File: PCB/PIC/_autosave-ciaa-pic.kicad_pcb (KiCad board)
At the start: 4 copper layers, 138.8 x 86.3 mm, 442 parts, among them IC1 PS2805-4, IC2 PS2805-4, J1 TB_1X3, J10 TB_1X3, J11 TB_1X2, J12 TB_1X3, J13 TB_1X3, J14 TB_1X2, J15 TB_1X3, J16 TB_1X3, J17 TB_1X2, J18 TB_1X2, J19 TB_1X2, J2 TB_1X3, J3 DB9, J4 TB_1X3, J5 RJ45-TRANSFO, J6 ZX62-AB-5PA, J7 ZX62-AB-5PA, J8 TB_1X3, J9 TB_1X3, K1 RELAY_G5V-2, K2 RELAY_G5V-2, K3 RELAY_G5V-2, K4 RELAY_G5V-2, P1 CONN_6X2, P14 SPI, P2 CONN_6X2, P3 CONN_5, P4 CONN_6, P6 CONN_4X2, Q1 PBSS5240XF, Q11 NDS7002A, Q12 NDS7002A, Q14 BC817-40, Q2 FQT13N06L, Q3 FQT13N06L, Q4 FQT13N06L, Q5 FQT13N06L, Q6 NDS7002A, Q7 NDS7002A, SW1 SW_PUSH_4, U1 LAN_8740, U10 MIC2025-2YM, U11 MCP6024, U12 24AA1025, U13 24AA025E48, U14 TXB0108, U15 TPS2051B, U16 PIC32MZ2048EC, U17 FT2232H, U18 LM358, U19 93C46, U2 SI502, U20 SST26VF064BA, U21 MCP6022, U22 ASDMB-24.000MHZ-LC-T, U23 MCP1416, U24 23A1024, U25 TC25L5I32K7680, U26 MCP9700, U27 MCP1416, U28 MCP1416, U29 MCP1416, U3 LM2596-5.0, U4 NCP1117ST33T3G, U5 MAX3072, U6 ST3232E, U7 VP231, U8 PESD1CAN, U9 PRTR5V0U2X, X1 12MHz

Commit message: rev02 aignacion footprint
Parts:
- removed P2: CONN_6X2, PIN_ARRAY_6X2
- removed REF**: Symbol_OSHW-Logo_CopperTop, Symbols:Symbol_OSHW-Logo_CopperTop
- removed REF**: Symbol_ESD-Logo_CopperTop, Symbols:Symbol_ESD-Logo_CopperTop
- added F1, F2, F3: FIDUCIAL, Fiducials:Fiducial_Modern_CopperTop, F.Cu at (84.6, 110.0)
- added F4, F5, F6: FIDUCIAL, Fiducials:Fiducial_Modern_CopperBottom, F.Cu at (84.6, 110.0)
- C10, C101, C11, C12, C13, C14, C15, C19, C2, C20, C22, C23, C24, C25, C26, C27, C29, C3, C30, C32, C33, C35, C36, C37, C38, C39, C4, C40, C41, C42, C43, C44, C45, C47, C48, C49, C50, C51, C52, C53, C54, C55, C56, C57, C58, C59, C6, C61, C62, C63, C64, C65, C66, C67, C69, C7, C70, C71, C72, C73, C74, C75, C76, C77, C79, C81, C82, C83, C84, C85, C86, C87, C89, C90, C91, C92, C93, C94, C98, C99: footprint c_0603 -> Capacitors_SMD:C_0603
- C21, C28: value 10uF / 6V3 -> 10uF/6V3
- C31: footprint c_1206_tantalio_1 -> Capacitors_SMD:C_0603
- C46, C88: footprint SMC0603 -> Capacitors_SMD:C_0603
- GS10, GS6, GS7, GS8, GS9: footprint GS3 -> footprints:GS3
- GS3, GS4: footprint GS2 -> footprints:GS2
- IC1, IC2: footprint -SOP16 -> footprints:-SOP16
- J1, J10, J12, J13, J15, J16, J2, J4, J8, J9: footprint bornier3 -> footprints:bornier3
- J11, J14, J17, J18, J19: footprint bornier2 -> footprints:bornier2
- J3: footprint K22X-E9P-NJ -> footprints:K22X-E9P-NJ
- J5: footprint RJ45_TRANSFO -> footprints:RJ45_TRANSFO
- J6, J7: footprint USB_microAB_ZX62-AB&B-5PA-11 -> footprints:USB_microAB_ZX62-AB&B-5PA-11
- K1, K2, K3, K4: footprint G5V-2 -> footprints:G5V-2
- P4: footprint PIN_ARRAY_6X1 -> footprints:PIN_ARRAY_6X1
- Q14: footprint -SOT23 -> footprints:SOT23
- Q2, Q3, Q4, Q5: footprint SOT223_Opendous -> footprints:SOT223
- R1, R10, R100, R101, R102, R103, R104, R106, R108, R11, R110, R111, R112, R114, R115, R116, R117, R118, R119, R12, R120, R121, R122, R123, R124, R125, R126, R127, R128, R129, R13, R130, R131, R132, R133, R134, R135, R136, R137, R138, R14, R15, R16, R17, R18, R19, R2, R20, R21, R22, R23, R24, R25, R26, R27, R28, R29, R3, R30, R32, R33, R34, R35, R36, R37, R38, R39, R4, R41, R43, R44, R46, R47, R48, R49, R5, R50, R51, R52, R53, R54, R55, R56, R57, R58, R59, R6, R60, R61, R62, R63, R64, R65, R66, R67, R68, R69, R7, R70, R71, R72, R73, R74, R75, R76, R77, R78, R79, R8, R84, R85, R86, R87, R88, R89, R9, R90, R91, R92, R93, R94, R95, R96, R97, R98, R99: footprint SM0603_Resistor -> Resistors_SMD:R_0603
- R105, R107, R109, R113, R139, R140, R141, R142, R143, R144, R145, R146, R147, R148, R149, R150, R153, R154, R155, R156, R157, R158, R159, R160, R161, R162, R163, R164, R165, R31, R80, R81, R82, R83: footprint SM0603 -> Resistors_SMD:R_0603
- R40: footprint SM0603_Resistor -> Resistors_SMD:R_1206
- TH4, TH5, TH6, TH7: footprint MF-USMF -> footprints:MF-USMF
- U1: footprint QFN32_Opendous -> footprints:QFN32_Opendous
- U14: footprint tssop-20 -> footprints:tssop-20
- U16: footprint LQFP144-M05 -> footprints:LQFP144-M05
- U17: footprint LQFP64-M05 -> footprints:LQFP64-M05
- U19, U7: footprint -SOIC8 -> footprints:-SOIC8
- U2, U22, U25: footprint 4SMD -> footprints:4SMD
- U23, U27, U28, U29: footprint SOT23-5 -> footprints:SOT23-5
- U24: footprint SO8E -> footprints:-SOIC8
- U26: footprint SOT23 -> footprints:SOT23
- U5: footprint -SOIC8 -> SMD_Packages:SOIC-8-N
- U8: footprint SOT23-3 -> footprints:SOT23
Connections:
- net /CPU/EECLK renamed /JTAG/EECLK
- net /CPU/EECS renamed /JTAG/EECS
- net /CPU/EEDATA renamed /JTAG/EEDATA
- net /CPU/FT_OE renamed /JTAG/FT_OE
- net /CPU/FT_RST renamed /JTAG/FT_RST
- net /CPU/FT_TCK renamed /JTAG/FT_TCK
- net /CPU/FT_TDI renamed /JTAG/FT_TDI
- net /CPU/FT_TDO renamed /JTAG/FT_TDO
- net /CPU/FT_TMS renamed /JTAG/FT_TMS
- net /CPU/FT_TRST renamed /JTAG/FT_TRST
- net /CPU/FT_XTIN renamed /JTAG/FT_XTIN
- net /CPU/FT_XTOUT renamed /JTAG/FT_XTOUT
- net /CPU/RST renamed /JTAG/RST
- net /CPU/TRST renamed /JTAG/TRST
- net /CPU/USB_DEBUG_VBUS renamed /JTAG/USB_DEBUG_VBUS
- net /CPU/USB_JTAG_1.8V renamed /JTAG/USB_JTAG_1.8V
- net /CPU/USB_JTAG_DM renamed /JTAG/USB_JTAG_DM
- net /CPU/USB_JTAG_DP renamed /JTAG/USB_JTAG_DP
- net N-00000244 renamed /Ethernet/RXP
- net N-00000246 renamed /Ethernet/TXD0
- net N-00000247 renamed /Ethernet/TXD1
- net N-00000248 renamed /Ethernet/TXEN
- net N-00000250 renamed /Ethernet/MDC
- net N-00000253 renamed /Ethernet/RXER
- net N-00000257 renamed /Ethernet/XTAL1
- net N-00000259 renamed /Ethernet/RXD2
- net N-00000261 renamed /Ethernet/RXD0
- net N-00000262 renamed /Ethernet/RXCLK
- net N-00000263 renamed /Ethernet/RXD3
- net N-00000265 renamed /Ethernet/TXP
- net N-00000266 renamed /Ethernet/TXN
- net N-00000267 renamed /Ethernet/CRS_DV
- net N-00000268 renamed /Ethernet/RXN
- net N-00000269 renamed /Ethernet/MDIO
- net N-00000270 renamed /Ethernet/RXD1
- C1 pad 1: N-00000271 -> /Ethernet/+Filter
- C10 pad 1: N-00000271 -> /Ethernet/+Filter
- C2 pad 1: N-00000271 -> /Ethernet/+Filter
- C3 pad 1: N-00000271 -> /Ethernet/+Filter
- C5 pad 1: N-00000271 -> /Ethernet/+Filter
- C6 pad 1: N-00000271 -> /Ethernet/+Filter
- GS3 pad 2: /CPU/RESET -> (no net)
- GS4 pad 2: /Memorias NV/SPIFI_CLK -> (no net)
- J5 pad 2: N-00000271 -> /Ethernet/+Filter
- J5 pad 5: N-00000271 -> /Ethernet/+Filter
- K1 pad 4: /Salidas Digitales/C1B -> (no net)
- K1 pad 6: /Salidas Digitales/NC1B -> (no net)
- K1 pad 8: /Salidas Digitales/NO1B -> (no net)
- K2 pad 4: /Salidas Digitales/C3B -> (no net)
- K2 pad 6: /Salidas Digitales/NC3B -> (no net)
- K2 pad 8: /Salidas Digitales/NO3B -> (no net)
- K3 pad 4: /Salidas Digitales/C2B -> (no net)
- K3 pad 6: /Salidas Digitales/NC2B -> (no net)
- K3 pad 8: /Salidas Digitales/NO2B -> (no net)
- K4 pad 4: /Salidas Digitales/C4B -> (no net)
- K4 pad 6: /Salidas Digitales/NC4B -> (no net)
- K4 pad 8: /Salidas Digitales/NO4B -> (no net)
- L1 pad 1: +3.3V -> /Ethernet/+Filter
- L1 pad 2: N-00000271 -> +3.3V
- R3 pad 1: N-00000271 -> /Ethernet/+Filter
- R4 pad 1: N-00000271 -> /Ethernet/+Filter
- R5 pad 1: N-00000271 -> /Ethernet/+Filter
- R6 pad 1: N-00000271 -> /Ethernet/+Filter
- R98 pad 1: +3.3V -> Net-(R98-Pad1)
- R98 pad 2: N-0000097 -> +3.3V
- U1 pad 1: N-00000271 -> /Ethernet/+Filter
- U1 pad 27: N-00000271 -> /Ethernet/+Filter
- U14 pad 16: /CPU/TMS -> (no net)
- U14 pad 17: /CPU/TDO -> (no net)
- U14 pad 18: /CPU/TDI -> (no net)
- U14 pad 20: /CPU/TCK -> (no net)
- U16 pad 104: /CPU/U2_TXD -> (no net)
- U16 pad 22: /CPU/TMS -> (no net)
- U16 pad 23: /USB OTG/USB0_PWR_FAULT -> (no net)
- U16 pad 56: /CPU/TCK -> (no net)
- U16 pad 57: /CPU/TDI -> (no net)
- U16 pad 58: /CPU/TDO -> (no net)
- U16 pad 80: /CPU/U2_RXD -> (no net)
- U17 pad 14: N-0000097 -> Net-(R98-Pad1)
- U17 pad 38: /CPU/U2_RXD -> (no net)
- U17 pad 39: /CPU/U2_TXD -> (no net)
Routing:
- net (no net): track 0.08 -> 486.7 mm, vias 0 -> 23
- net GND: track 490.0 -> 591.3 mm, vias 114 -> 109
- net N-00000271: track 79.1 -> 0.00 mm, vias 5 -> 0
- net +3.3V: track 261.1 -> 329.7 mm, vias 65 -> 80
- net /Ethernet/+Filter: track 0.00 -> 49.6 mm, vias 0 -> 2
- net /CPU/U2_TXD: track 47.7 -> 0.00 mm, vias 1 -> 0
- net /CPU/TMS: track 45.6 -> 0.00 mm, vias 4 -> 0
- net /CPU/U2_RXD: track 43.5 -> 0.00 mm, vias 1 -> 0
- net GNDA: track 132.6 -> 176.0 mm, vias 28 -> 25
- net /CPU/TDI: track 36.3 -> 0.00 mm, vias 2 -> 0
- net /CPU/TCK: track 35.7 -> 0.00 mm, vias 2 -> 0
- net /Salidas Digitales/C4B: track 34.9 -> 0.00 mm, vias 3 -> 0
- net /Salidas Digitales/NC4B: track 33.6 -> 0.00 mm, vias 1 -> 0
- net /CPU/TDO: track 33.3 -> 0.00 mm, vias 2 -> 0
- net /Salidas Digitales/NC1B: track 27.4 -> 0.00 mm
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- added copper zone on Inner2.Cu, net /CPU/USB_JTAG_1.8V
- added copper zone on F.Cu, net N-00000168
- added copper zone on F.Cu, net N-00000211
- added copper zone on F.Cu, net N-00000214
- added copper zone on B.Cu, net N-00000225
- added copper zone on B.Cu, net N-00000226
- added copper zone on B.Cu, net N-00000239
- added copper zone on B.Cu, net N-00000240
- added copper zone on F.Cu, net N-00000240
- added copper zone on B.Cu, net N-00000241
- added copper zone on F.Cu, net N-00000241
- added copper zone on B.Cu, net N-00000356
- added copper zone on F.Cu, net N-00000373
- added copper zone on F.Cu, net N-00000374
- added copper zone on F.Cu, net N-00000375
- added copper zone on F.Cu, net N-00000376
- added copper zone on F.Cu, net N-00000377
- added copper zone on F.Cu, net N-00000378
- added copper zone on F.Cu, net N-00000379
- added copper zone on F.Cu, net N-00000390
- removed copper zone on Inner2.Cu, net /JTAG/USB_JTAG_1.8V
- removed copper zone on B.Cu, net Net-(C16-Pad1)
- removed copper zone on F.Cu, net Net-(C16-Pad1)
- removed copper zone on F.Cu, net Net-(C25-Pad1)
- removed copper zone on F.Cu, net Net-(C26-Pad1)
- removed copper zone on B.Cu, net Net-(D2-Pad1)
- removed copper zone on B.Cu, net Net-(D3-Pad2)
- removed copper zone on F.Cu, net Net-(D3-Pad2)
- removed copper zone on F.Cu, net Net-(FB7-Pad1)
- removed copper zone on F.Cu, net Net-(J13-Pad1)
- removed copper zone on F.Cu, net Net-(J13-Pad2)
- removed copper zone on B.Cu, net Net-(J15-Pad1)
- removed copper zone on F.Cu, net Net-(J15-Pad2)
- removed copper zone on F.Cu, net Net-(J15-Pad3)
- removed copper zone on B.Cu, net Net-(J2-Pad1)
- removed copper zone on B.Cu, net Net-(J2-Pad2)
- removed copper zone on F.Cu, net Net-(Q2-Pad4)
- removed copper zone on F.Cu, net Net-(Q3-Pad4)
- removed copper zone on F.Cu, net Net-(Q4-Pad4)
- removed copper zone on F.Cu, net Net-(Q5-Pad4)

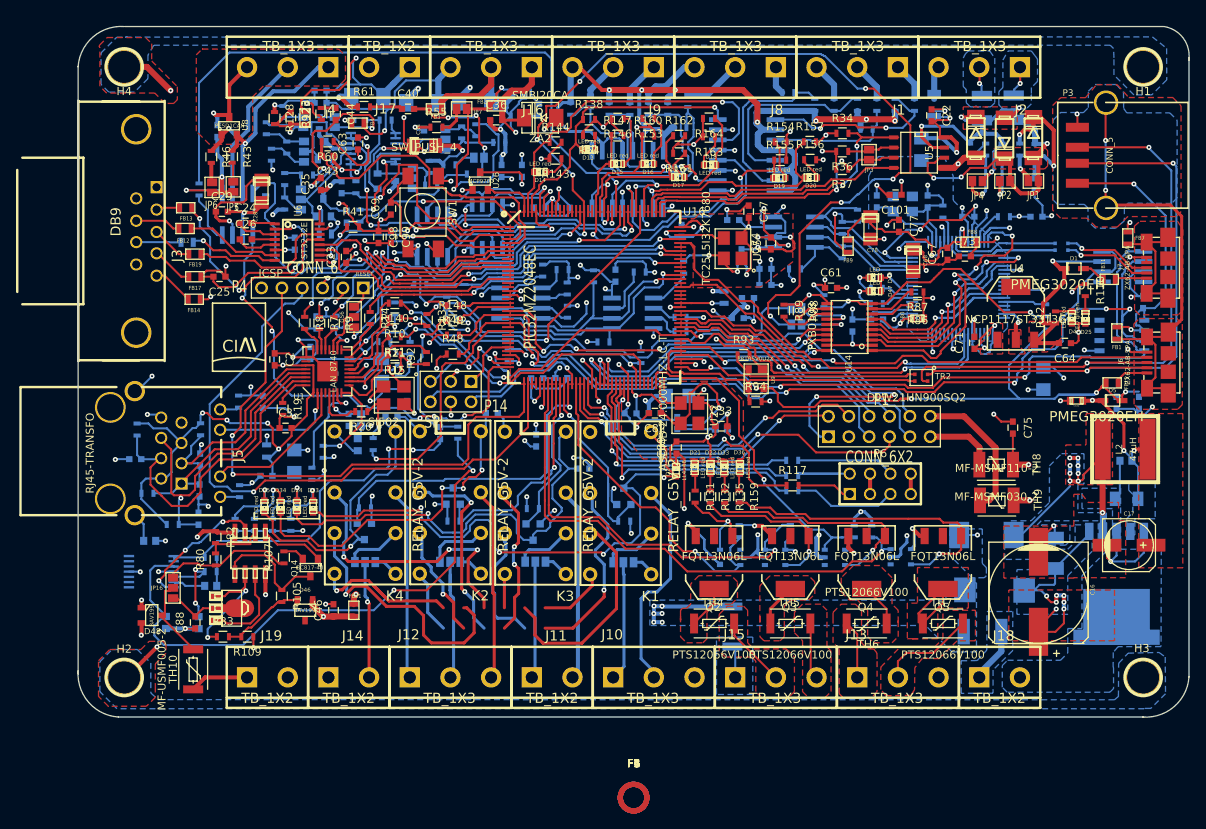
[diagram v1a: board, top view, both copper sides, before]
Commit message: rev02 se completa campo num. de frabicante(#manf) CIAA-PIC
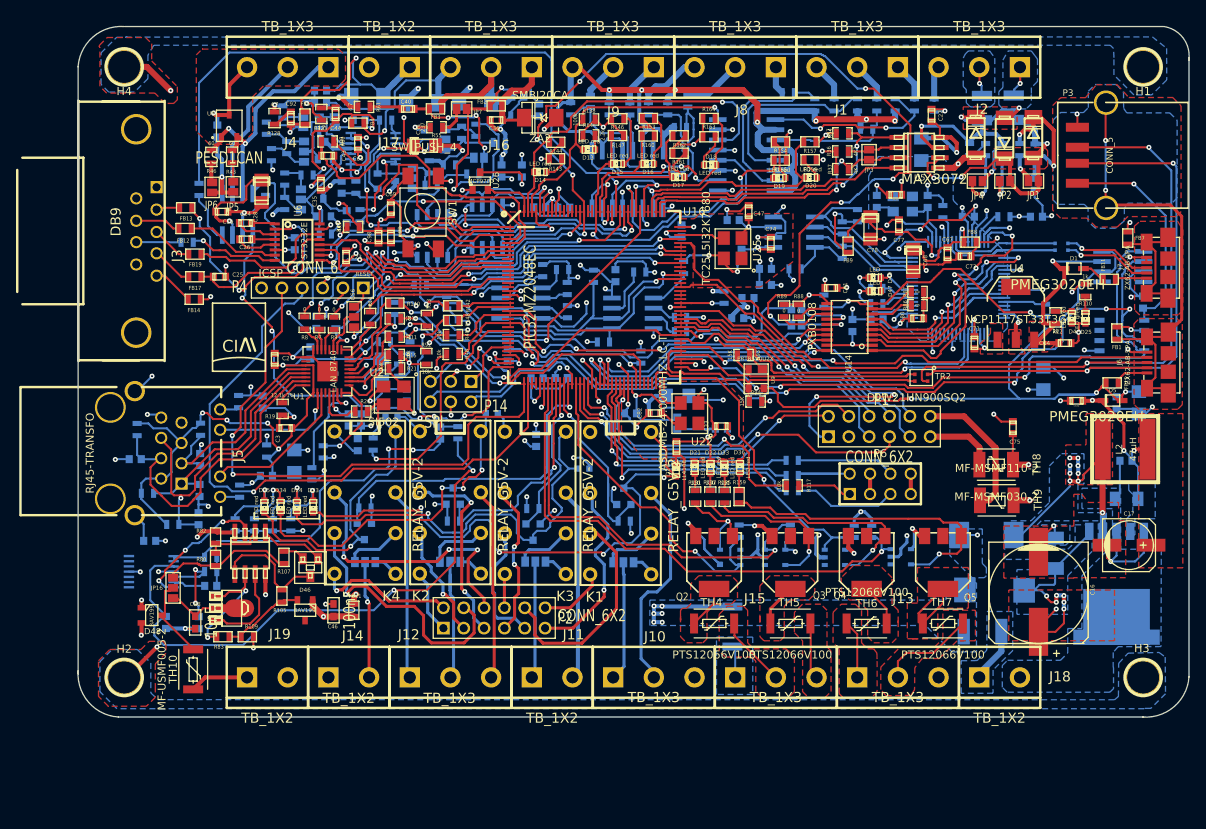
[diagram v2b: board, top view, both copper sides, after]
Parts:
- removed F1, F2, F3: FIDUCIAL, Fiducials:Fiducial_Modern_CopperTop
- removed F4, F5, F6: FIDUCIAL, Fiducials:Fiducial_Modern_CopperBottom
- added P2: CONN_6X2, PIN_ARRAY_6X2, F.Cu at (67.2, 87.6)
- C10, C101, C11, C12, C13, C14, C15, C19, C2, C20, C22, C23, C24, C25, C26, C27, C29, C3, C30, C32, C33, C35, C36, C37, C38, C39, C4, C40, C41, C42, C43, C44, C45, C47, C48, C49, C50, C51, C52, C53, C54, C55, C56, C57, C58, C59, C6, C61, C62, C63, C64, C65, C66, C67, C69, C7, C70, C71, C72, C73, C74, C75, C76, C77, C79, C81, C82, C83, C84, C85, C86, C87, C89, C90, C91, C92, C93, C94, C98, C99: footprint Capacitors_SMD:C_0603 -> c_0603
- C21, C28: value 10uF/6V3 -> 10uF / 6V3
- C31: footprint Capacitors_SMD:C_0603 -> c_1206_tantalio_1
- C46, C88: footprint Capacitors_SMD:C_0603 -> SMC0603
- GS10, GS6, GS7, GS8, GS9: footprint footprints:GS3 -> GS3
- GS3, GS4: footprint footprints:GS2 -> GS2
- IC1, IC2: footprint footprints:-SOP16 -> -SOP16
- J1, J10, J12, J13, J15, J16, J2, J4, J8, J9: footprint footprints:bornier3 -> bornier3
- J11, J14, J17, J18, J19: footprint footprints:bornier2 -> bornier2
- J3: footprint footprints:K22X-E9P-NJ -> K22X-E9P-NJ
- J5: footprint footprints:RJ45_TRANSFO -> RJ45_TRANSFO
- J6, J7: footprint footprints:USB_microAB_ZX62-AB&B-5PA-11 -> USB_microAB_ZX62-AB&B-5PA-11
- K1, K2, K3, K4: footprint footprints:G5V-2 -> G5V-2
- P4: footprint footprints:PIN_ARRAY_6X1 -> PIN_ARRAY_6X1
- Q14: footprint footprints:SOT23 -> -SOT23
- Q2, Q3, Q4, Q5: footprint footprints:SOT223 -> SOT223_Opendous
- R1, R10, R100, R101, R102, R103, R104, R106, R108, R11, R110, R111, R112, R114, R115, R116, R117, R118, R119, R12, R120, R121, R122, R123, R124, R125, R126, R127, R128, R129, R13, R130, R131, R132, R133, R134, R135, R136, R137, R138, R14, R15, R16, R17, R18, R19, R2, R20, R21, R22, R23, R24, R25, R26, R27, R28, R29, R3, R30, R32, R33, R34, R35, R36, R37, R38, R39, R4, R41, R43, R44, R46, R47, R48, R49, R5, R50, R51, R52, R53, R54, R55, R56, R57, R58, R59, R6, R60, R61, R62, R63, R64, R65, R66, R67, R68, R69, R7, R70, R71, R72, R73, R74, R75, R76, R77, R78, R79, R8, R84, R85, R86, R87, R88, R89, R9, R90, R91, R92, R93, R94, R95, R96, R97, R98, R99: footprint Resistors_SMD:R_0603 -> SM0603_Resistor
- R105, R107, R109, R113, R139, R140, R141, R142, R143, R144, R145, R146, R147, R148, R149, R150, R153, R154, R155, R156, R157, R158, R159, R160, R161, R162, R163, R164, R165, R31, R80, R81, R82, R83: footprint Resistors_SMD:R_0603 -> SM0603
- R40: footprint Resistors_SMD:R_1206 -> SM0603_Resistor
- TH4, TH5, TH6, TH7: footprint footprints:MF-USMF -> MF-USMF
- U1: footprint footprints:QFN32_Opendous -> QFN32_Opendous
- U14: footprint footprints:tssop-20 -> tssop-20
- U16: footprint footprints:LQFP144-M05 -> LQFP144-M05
- U17: footprint footprints:LQFP64-M05 -> LQFP64-M05
- U19, U7: footprint footprints:-SOIC8 -> -SOIC8
- U2, U22, U25: footprint footprints:4SMD -> 4SMD
- U23, U27, U28, U29: footprint footprints:SOT23-5 -> SOT23-5
- U24: footprint footprints:-SOIC8 -> SO8E
- U26: footprint footprints:SOT23 -> SOT23
- U5: footprint SMD_Packages:SOIC-8-N -> -SOIC8
- U8: footprint footprints:SOT23 -> SOT23-3
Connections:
- net /Ethernet/CRS_DV renamed N-00000267
- net /Ethernet/MDC renamed N-00000250
- net /Ethernet/MDIO renamed N-00000269
- net /Ethernet/RXCLK renamed N-00000262
- net /Ethernet/RXD0 renamed N-00000261
- net /Ethernet/RXD1 renamed N-00000270
- net /Ethernet/RXD2 renamed N-00000259
- net /Ethernet/RXD3 renamed N-00000263
- net /Ethernet/RXER renamed N-00000253
- net /Ethernet/RXN renamed N-00000268
- net /Ethernet/RXP renamed N-00000244
- net /Ethernet/TXD0 renamed N-00000246
- net /Ethernet/TXD1 renamed N-00000247
- net /Ethernet/TXEN renamed N-00000248
- net /Ethernet/TXN renamed N-00000266
- net /Ethernet/TXP renamed N-00000265
- net /Ethernet/XTAL1 renamed N-00000257
- net /JTAG/EECLK renamed /CPU/EECLK
- net /JTAG/EECS renamed /CPU/EECS
- net /JTAG/EEDATA renamed /CPU/EEDATA
- net /JTAG/FT_OE renamed /CPU/FT_OE
- net /JTAG/FT_RST renamed /CPU/FT_RST
- net /JTAG/FT_TCK renamed /CPU/FT_TCK
- net /JTAG/FT_TDI renamed /CPU/FT_TDI
- net /JTAG/FT_TDO renamed /CPU/FT_TDO
- net /JTAG/FT_TMS renamed /CPU/FT_TMS
- net /JTAG/FT_TRST renamed /CPU/FT_TRST
- net /JTAG/FT_XTIN renamed /CPU/FT_XTIN
- net /JTAG/FT_XTOUT renamed /CPU/FT_XTOUT
- net /JTAG/RST renamed /CPU/RST
- net /JTAG/TRST renamed /CPU/TRST
- net /JTAG/USB_DEBUG_VBUS renamed /CPU/USB_DEBUG_VBUS
- net /JTAG/USB_JTAG_DM renamed /CPU/USB_JTAG_DM
- net /JTAG/USB_JTAG_DP renamed /CPU/USB_JTAG_DP
- C1 pad 1: /Ethernet/+Filter -> N-00000271
- C10 pad 1: /Ethernet/+Filter -> N-00000271
- C2 pad 1: /Ethernet/+Filter -> N-00000271
- C3 pad 1: /Ethernet/+Filter -> N-00000271
- C5 pad 1: /Ethernet/+Filter -> N-00000271
- C6 pad 1: /Ethernet/+Filter -> N-00000271
- C70 pad 1: /JTAG/USB_JTAG_1.8V -> /CPU/USB_JTAG_1.8V
- C71 pad 1: /JTAG/USB_JTAG_1.8V -> /CPU/USB_JTAG_1.8V
- C72 pad 1: /JTAG/USB_JTAG_1.8V -> /CPU/USB_JTAG_1.8V
- C80 pad 1: /JTAG/USB_JTAG_1.8V -> /CPU/USB_JTAG_1.8V
- GS3 pad 2: (no net) -> /CPU/RESET
- GS4 pad 2: (no net) -> /Memorias NV/SPIFI_CLK
- J5 pad 2: /Ethernet/+Filter -> N-00000271
- J5 pad 5: /Ethernet/+Filter -> N-00000271
- K1 pad 4: (no net) -> /Salidas Digitales/C1B
- K1 pad 6: (no net) -> /Salidas Digitales/NC1B
- K1 pad 8: (no net) -> /Salidas Digitales/NO1B
- K2 pad 4: (no net) -> /Salidas Digitales/C3B
- K2 pad 6: (no net) -> /Salidas Digitales/NC3B
- K2 pad 8: (no net) -> /Salidas Digitales/NO3B
- K3 pad 4: (no net) -> /Salidas Digitales/C2B
- K3 pad 6: (no net) -> /Salidas Digitales/NC2B
- K3 pad 8: (no net) -> /Salidas Digitales/NO2B
- K4 pad 4: (no net) -> /Salidas Digitales/C4B
- K4 pad 6: (no net) -> /Salidas Digitales/NC4B
- K4 pad 8: (no net) -> /Salidas Digitales/NO4B
- L1 pad 1: /Ethernet/+Filter -> +3.3V
- L1 pad 2: +3.3V -> N-00000271
- R3 pad 1: /Ethernet/+Filter -> N-00000271
- R4 pad 1: /Ethernet/+Filter -> N-00000271
- R5 pad 1: /Ethernet/+Filter -> N-00000271
- R6 pad 1: /Ethernet/+Filter -> N-00000271
- R98 pad 1: Net-(R98-Pad1) -> +3.3V
- R98 pad 2: +3.3V -> N-0000097
- U1 pad 1: /Ethernet/+Filter -> N-00000271
- U1 pad 27: /Ethernet/+Filter -> N-00000271
- U14 pad 16: (no net) -> /CPU/TMS
- U14 pad 17: (no net) -> /CPU/TDO
- U14 pad 18: (no net) -> /CPU/TDI
- U14 pad 20: (no net) -> /CPU/TCK
- U16 pad 104: (no net) -> /CPU/U2_TXD
- U16 pad 22: (no net) -> /CPU/TMS
- U16 pad 23: (no net) -> /USB OTG/USB0_PWR_FAULT
- U16 pad 56: (no net) -> /CPU/TCK
- U16 pad 57: (no net) -> /CPU/TDI
- U16 pad 58: (no net) -> /CPU/TDO
- U16 pad 80: (no net) -> /CPU/U2_RXD
- U17 pad 12: /JTAG/USB_JTAG_1.8V -> /CPU/USB_JTAG_1.8V
- U17 pad 14: Net-(R98-Pad1) -> N-0000097
- U17 pad 37: /JTAG/USB_JTAG_1.8V -> /CPU/USB_JTAG_1.8V
- U17 pad 38: (no net) -> /CPU/U2_RXD
- U17 pad 39: (no net) -> /CPU/U2_TXD
- U17 pad 49: /JTAG/USB_JTAG_1.8V -> /CPU/USB_JTAG_1.8V
- U17 pad 64: /JTAG/USB_JTAG_1.8V -> /CPU/USB_JTAG_1.8V
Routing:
- net (no net): track 486.7 -> 0.08 mm, vias 23 -> 0
- net GND: track 591.3 -> 490.0 mm, vias 109 -> 114
- net N-00000271: track 0.00 -> 79.1 mm, vias 0 -> 5
- net +3.3V: track 329.7 -> 261.1 mm, vias 80 -> 65
- net /Ethernet/+Filter: track 49.6 -> 0.00 mm, vias 2 -> 0
- net /CPU/U2_TXD: track 0.00 -> 47.7 mm, vias 0 -> 1
- net /CPU/TMS: track 0.00 -> 45.6 mm, vias 0 -> 4
- net /CPU/U2_RXD: track 0.00 -> 43.5 mm, vias 0 -> 1
- net GNDA: track 176.0 -> 132.6 mm, vias 25 -> 28
- net /CPU/TDI: track 0.00 -> 36.3 mm, vias 0 -> 2
- net /CPU/TCK: track 0.00 -> 35.7 mm, vias 0 -> 2
- net /Salidas Digitales/C4B: track 0.00 -> 34.9 mm, vias 0 -> 3
- net /JTAG/USB_JTAG_1.8V: track 34.3 -> 0.00 mm, vias 5 -> 0
- net /Salidas Digitales/NC4B: track 0.00 -> 33.6 mm, vias 0 -> 1
- net /CPU/TDO: track 0.00 -> 33.3 mm, vias 0 -> 2
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- added copper zone on F.Cu, net N-00000168
- added copper zone on F.Cu, net N-00000211
- added copper zone on F.Cu, net N-00000214
- added copper zone on B.Cu, net N-00000225
- added copper zone on B.Cu, net N-00000226
- added copper zone on B.Cu, net N-00000239
- added copper zone on B.Cu, net N-00000240
- added copper zone on F.Cu, net N-00000240
- added copper zone on B.Cu, net N-00000241
- added copper zone on F.Cu, net N-00000241
- added copper zone on B.Cu, net N-00000356
- added copper zone on F.Cu, net N-00000373
- added copper zone on F.Cu, net N-00000374
- added copper zone on F.Cu, net N-00000375
- added copper zone on F.Cu, net N-00000376
- added copper zone on F.Cu, net N-00000377
- added copper zone on F.Cu, net N-00000378
- added copper zone on F.Cu, net N-00000379
- added copper zone on F.Cu, net N-00000390
- removed copper zone on F.Cu, net N-00000168 (its old number)
- removed copper zone on F.Cu, net N-00000211 (its old number)
- removed copper zone on F.Cu, net N-00000214 (its old number)
- removed copper zone on B.Cu, net N-00000225 (its old number)
- removed copper zone on B.Cu, net N-00000226 (its old number)
- removed copper zone on B.Cu, net N-00000239 (its old number)
- removed copper zone on B.Cu, net N-00000240 (its old number)
- removed copper zone on F.Cu, net N-00000240 (its old number)
- removed copper zone on B.Cu, net N-00000241 (its old number)
- removed copper zone on F.Cu, net N-00000241 (its old number)
- removed copper zone on B.Cu, net N-00000356 (its old number)
- removed copper zone on F.Cu, net N-00000373 (its old number)
- removed copper zone on F.Cu, net N-00000374 (its old number)
- removed copper zone on F.Cu, net N-00000375 (its old number)
- removed copper zone on F.Cu, net N-00000376 (its old number)
- removed copper zone on F.Cu, net N-00000377 (its old number)
- removed copper zone on F.Cu, net N-00000378 (its old number)
- removed copper zone on F.Cu, net N-00000379 (its old number)
- removed copper zone on F.Cu, net N-00000390 (its old number)

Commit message: BOM File CIAA-PIC
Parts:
- removed C64, C65: 100nF, c_0603
- removed P2: CONN_6X2, PIN_ARRAY_6X2
- removed R25, R26, R27, R28, R29, R30: 0, SM0603_Resistor
- removed U15: TPS2051B, so-8
- added F1: FIDUCIAL, Fiducials:Fiducial_1mm_Dia_2.54mm_Outer_CopperTop, F.Cu at (123.8, 72.4)
- added F2: FIDUCIAL, Fiducials:Fiducial_1mm_Dia_2.54mm_Outer_CopperTop, F.Cu at (28.9, 54.3)
- added F3: FIDUCIAL, Fiducials:Fiducial_1mm_Dia_2.54mm_Outer_CopperTop, F.Cu at (139.6, 18.9)
- added F4: FIDUCIAL, Fiducials:Fiducial_1mm_Dia_2.54mm_Outer_CopperBottom, F.Cu at (123.9, 72.2)
- added F5: FIDUCIAL, Fiducials:Fiducial_1mm_Dia_2.54mm_Outer_CopperBottom, F.Cu at (139.9, 18.9)
- added F6: FIDUCIAL, Fiducials:Fiducial_1mm_Dia_2.54mm_Outer_CopperBottom, F.Cu at (29.1, 54.0)
- C1, C18, C31, C34, C78: footprint c_1206_tantalio_1 -> footprints:c_1206_tantalio
- C10, C100, C101, C102, C103, C104, C11, C12, C13, C14, C15, C19, C2, C20, C22, C23, C24, C25, C26, C27, C29, C3, C30, C32, C33, C35, C36, C37, C38, C39, C4, C40, C41, C42, C43, C44, C45, C47, C48, C49, C50, C51, C52, C53, C54, C55, C56, C57, C58, C59, C6, C61, C62, C63, C67, C69, C7, C70, C71, C72, C73, C74, C75, C76, C77, C82, C83, C84, C85, C86, C87, C89, C90, C91, C92, C93, C94, C98, C99: footprint c_0603 -> Capacitors_SMD:C_0603
- C16: footprint c_elec_13.7x13x13.5 -> footprints:c_elec_13.7x13x13.5
- C17: footprint c_elec_6.3x7.7 -> footprints:c_elec_6.3x7.7
- C21, C28: value 10uF / 6V3 -> 10uF/6V3; footprint c_1206_tantalio -> footprints:c_1206_tantalio
- C46, C88: footprint SMC0603 -> Capacitors_SMD:C_0603
- C5: footprint c_1206_tantalio_1 -> footprints:c_0603
- C60: footprint c_1206_tantalio -> footprints:c_0603
- C66: value 10nF -> 100nF; footprint c_0603 -> Capacitors_SMD:C_0603
- C68: footprint c_1206_tantalio -> footprints:c_1206_tantalio
- C79, C81: value 27p -> 12p; footprint c_0603 -> Capacitors_SMD:C_0603
- C8, C80, C9: footprint c_0603 -> footprints:c_0603
- D1, D5: footprint SOD323 -> footprints:SOD323
- D10, D11, D12, D9: footprint SOT23 -> footprints:SOT23-DIODE
- D13, D14, D15, D16, D17, D18, D19, D20, D21, D22, D23, D24, D25, D33, D34, D35, D36, D47, D49: footprint LED-0603 -> LEDs:LED_0603
- D2: footprint DO-214AB(SMC) -> Diodes_SMD:DO-214AB
- D3: footprint Diode-SMC_Standard_RevA_26July2010 -> footprints:DO-214AB(SMC)
- D4: footprint LED-0603 -> footprints:LED-0603
- D46: footprint SOT23-DIODE -> footprints:SOT23-DIODE
- D48: footprint SOT23-DIODE -> footprints:-SOT89
- D6, D7, D8: footprint DO214AA-1-2 -> footprints:DO214AA-1-2
- FB1, FB11, FB12, FB13, FB14, FB15, FB17, FB18, FB19, FB2, FB21, FB3, FB4, FB5, FB7, FB8, FB9, L1: footprint SM0603 -> footprints:SM0603
- FB20, FB6: footprint SM0603 -> footprints:SM0603_Resistor
- GS10, GS6, GS7, GS8, GS9, JP10, JP12, JP14, JP16, JP8: footprint GS3 -> footprints:GS3
- GS3, GS4, JP1, JP11, JP13, JP2, JP3, JP4, JP5, JP6, JP7, JP9: footprint GS2 -> footprints:GS2
- H1, H2, H3, H4: footprint 1pin -> footprints:1pin
- IC1, IC2: footprint -SOP16 -> footprints:-SOP16
- J1, J10, J12, J13, J15, J16, J2, J4, J8, J9: footprint bornier3 -> footprints:bornier3
- J11, J14, J17, J18, J19: footprint bornier2 -> footprints:bornier2
- J3: footprint K22X-E9P-NJ -> footprints:K22X-E9P-NJ
- J5: footprint RJ45_TRANSFO -> footprints:RJ45_TRANSFO
- J6, J7: footprint USB_microAB_ZX62-AB&B-5PA-11 -> footprints:USB_microAB_ZX62-AB&B-5PA-11
- K1, K2, K3, K4: footprint G5V-2 -> footprints:G5V-2
- L2: footprint Inductor_10x9.8mm -> footprints:Inductor_10x9.8mm
- P1: footprint PIN_ARRAY_6X2 -> footprints:PIN_ARRAY_6X2
- P14: footprint PIN_ARRAY_3X2 -> footprints:PIN_ARRAY_3X2
- P4: footprint PIN_ARRAY_6X1 -> footprints:PIN_ARRAY_6X1
- P6: footprint pin_array_4x2 -> footprints:pin_array_4x2
- PS1, PS2: footprint SM1210 -> footprints:MF-MSMF
- Q1: footprint -SOT89 -> footprints:-SOT89
- Q11, Q12, Q6, Q7: footprint SOT23GDS -> footprints:SOT23
- Q14: footprint -SOT23 -> footprints:SOT23
- Q2, Q3, Q4, Q5: footprint SOT223_Opendous -> footprints:SOT223
- R1, R10, R100, R101, R102, R103, R104, R106, R108, R11, R110, R111, R112, R114, R115, R116, R117, R118, R119, R12, R120, R121, R122, R123, R124, R125, R126, R127, R128, R129, R13, R130, R131, R132, R133, R134, R135, R136, R137, R138, R14, R15, R16, R17, R18, R19, R2, R20, R21, R22, R23, R24, R3, R33, R34, R36, R37, R38, R4, R41, R43, R44, R46, R47, R48, R49, R5, R50, R51, R52, R53, R54, R55, R56, R57, R58, R59, R6, R60, R61, R62, R63, R64, R7, R73, R74, R75, R76, R77, R78, R79, R8, R84, R85, R86, R87, R88, R89, R9, R90, R91, R92, R93, R94, R95, R97, R98, R99: footprint SM0603_Resistor -> Resistors_SMD:R_0603
- R105, R109, R113, R139, R140, R141, R142, R143, R144, R146, R147, R148, R149, R150, R153, R154, R155, R156, R157, R158, R159, R160, R161, R162, R163, R164, R165, R31, R80, R81, R82, R83: footprint SM0603 -> Resistors_SMD:R_0603
- R107: footprint SM0603 -> Resistors_SMD:R_1206
- R145: value 220 -> 270; footprint SM0603 -> Resistors_SMD:R_0603
- R32, R39: value 680 -> 390; footprint SM0603_Resistor -> Resistors_SMD:R_0603
- R35: value 120 -> 220; footprint SM0603_Resistor -> Resistors_SMD:R_0603
- R40: footprint SM0603_Resistor -> Resistors_SMD:R_2010
- R65, R66, R67, R68, R69, R70, R71, R72: footprint SM0603_Resistor -> Resistors_SMD:R_1206
- R96: value 220 -> 270; footprint SM0603_Resistor -> Resistors_SMD:R_0603
- SW1: footprint PUSH_SWITCH -> footprints:PUSH_SWITCH
- TH1: footprint MF-SM030 -> footprints:2-SMD-MF-SM030
- TH10, TH4, TH5, TH6, TH7: footprint MF-USMF -> footprints:MF-USMF
- TR1, TR2: footprint SRF2012 -> footprints:SRF2012
- U1: footprint QFN32_Opendous -> footprints:QFN32_Opendous
- U10, U19, U7: footprint -SOIC8 -> footprints:-SOIC8
- U11: footprint TSSOP14 -> footprints:TSSOP14
- U12, U13, U18, U5: footprint -SOIC8 -> SMD_Packages:SOIC-8-N
- U14: footprint tssop-20 -> footprints:tssop-20
- U16: footprint LQFP144-M05 -> footprints:LQFP144-M05
- U17: footprint LQFP64-M05 -> footprints:LQFP64-M05
- U2, U22, U25: footprint 4SMD -> footprints:4SMD
- U20: footprint SO8 -> footprints:SO8-sst
- U23, U27, U28, U29: footprint SOT23-5 -> footprints:SOT23-5
- U24: footprint SO8E -> footprints:-SOIC8
- U26: footprint SOT23 -> footprints:SOT23
- U3: footprint D2PACK5-LM2596 -> footprints:TO263-6--D2PACK5-LM2596
- U4: footprint SOT223 -> footprints:SOT223
- U6: footprint TSSOP16 -> footprints:TSSOP16
- U8: footprint SOT23-3 -> footprints:SOT23
- U9: footprint sot143B -> footprints:sot143B
- X1: footprint FA238V-XTAL -> footprints:4SMD
- ZA1: footprint DO-214AC(SMA) -> footprints:DO214AA-1-2
- ZA14: footprint SOD123F -> footprints:SOD123F
- ZA2, ZA3, ZA4, ZA5: footprint DO-214AA(SMB) -> footprints:DO-214AA(SMB)
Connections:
- net /CPU/EECLK renamed /JTAG/EECLK
- net /CPU/EECS renamed /JTAG/EECS
- net /CPU/EEDATA renamed /JTAG/EEDATA
- net /CPU/FT_OE renamed /JTAG/FT_OE
- net /CPU/FT_RST renamed /JTAG/FT_RST
- net /CPU/FT_TCK renamed /JTAG/FT_TCK
- net /CPU/FT_TDI renamed /JTAG/FT_TDI
- net /CPU/FT_TDO renamed /JTAG/FT_TDO
- net /CPU/FT_TMS renamed /JTAG/FT_TMS
- net /CPU/FT_TRST renamed /JTAG/FT_TRST
- net /CPU/FT_XTIN renamed /JTAG/FT_XTIN
- net /CPU/FT_XTOUT renamed /JTAG/FT_XTOUT
- net /CPU/RST renamed Net-(GS3-Pad1)
- net /CPU/TRST renamed Net-(GS4-Pad1)
- net /CPU/USB_DEBUG_VBUS renamed /JTAG/USB_DEBUG_VBUS
- net /CPU/USB_JTAG_1.8V renamed /JTAG/USB_JTAG_1.8V
- net /CPU/USB_JTAG_DM renamed /JTAG/USB_JTAG_DM
- net /CPU/USB_JTAG_DP renamed /JTAG/USB_JTAG_DP
- net /Entradas Digitales/IN0 renamed Net-(J1-Pad1)
- net /Entradas Digitales/IN1 renamed Net-(J1-Pad2)
- net /Entradas Digitales/IN2 renamed Net-(J1-Pad3)
- net /Entradas Digitales/IN3 renamed Net-(J8-Pad1)
- net /Entradas Digitales/IN4 renamed Net-(J8-Pad2)
- net /Entradas Digitales/IN5 renamed Net-(J8-Pad3)
- net /Entradas Digitales/IN6 renamed Net-(J9-Pad1)
- net /Entradas Digitales/IN7 renamed Net-(J9-Pad2)
- net N-00000246 renamed /Ethernet/TXD0
- net N-00000247 renamed /Ethernet/TXD1
- net N-00000248 renamed /Ethernet/TXEN
- net N-00000250 renamed /Ethernet/MDC
- net N-00000253 renamed /Ethernet/RXER
- net N-00000257 renamed /Ethernet/XTAL1
- net N-00000259 renamed /Ethernet/RXD2
- net N-00000261 renamed /Ethernet/RXD0
- net N-00000262 renamed /Ethernet/RXCLK
- net N-00000263 renamed /Ethernet/RXD3
- net N-00000267 renamed /Ethernet/CRS_DV
- net N-00000269 renamed /Ethernet/MDIO
- net N-00000270 renamed /Ethernet/RXD1
- C1 pad 1: N-00000271 -> /Ethernet/+Filter
- C10 pad 1: N-00000271 -> /Ethernet/+Filter
- C2 pad 1: N-00000271 -> /Ethernet/+Filter
- C3 pad 1: N-00000271 -> /Ethernet/+Filter
- C5 pad 1: N-00000271 -> /Ethernet/+Filter
- C6 pad 1: N-00000271 -> /Ethernet/+Filter
- D23 pad 2: N-00000355 -> Net-(D23-Pad2)
- D24 pad 2: N-00000367 -> Net-(D24-Pad2)
- D27 pad 1: N-00000355 -> Net-(D23-Pad2)
- D28 pad 1: N-00000367 -> Net-(D24-Pad2)
- D30 pad 1: N-00000371 -> Net-(D30-Pad1)
- D31 pad 1: N-00000370 -> Net-(D31-Pad1)
- D34 pad 2: N-00000371 -> Net-(D30-Pad1)
- D35 pad 2: N-00000370 -> Net-(D31-Pad1)
- FB1 pad 2: /USB OTG/GND_SH -> Net-(FB1-Pad2)
- J13 pad 3: (no net) -> GND
- J5 pad 2: N-00000271 -> /Ethernet/+Filter
- J5 pad 5: N-00000271 -> /Ethernet/+Filter
- J6 pad 2: /USB OTG/D- -> Net-(J6-Pad2)
- J6 pad 3: /USB OTG/D+ -> Net-(J6-Pad3)
- J6 pad 6: /USB OTG/GND_SH -> Net-(FB1-Pad2)
- J6 pad 7: /USB OTG/GND_SH -> Net-(FB1-Pad2)
- K1 pad 16: N-00000355 -> Net-(D23-Pad2)
- K1 pad 4: /Salidas Digitales/C1B -> (no net)
- K1 pad 6: /Salidas Digitales/NC1B -> (no net)
- K1 pad 8: /Salidas Digitales/NO1B -> (no net)
- K2 pad 16: N-00000371 -> Net-(D30-Pad1)
- K2 pad 4: /Salidas Digitales/C3B -> (no net)
- K2 pad 6: /Salidas Digitales/NC3B -> (no net)
- K2 pad 8: /Salidas Digitales/NO3B -> (no net)
- K3 pad 16: N-00000367 -> Net-(D24-Pad2)
- K3 pad 4: /Salidas Digitales/C2B -> (no net)
- K3 pad 6: /Salidas Digitales/NC2B -> (no net)
- K3 pad 8: /Salidas Digitales/NO2B -> (no net)
- K4 pad 16: N-00000370 -> Net-(D31-Pad1)
- K4 pad 4: /Salidas Digitales/C4B -> (no net)
- K4 pad 6: /Salidas Digitales/NC4B -> (no net)
- K4 pad 8: /Salidas Digitales/NO4B -> (no net)
- L1 pad 1: +3.3V -> /Ethernet/+Filter
- L1 pad 2: N-00000271 -> +3.3V
- P3 pad 1: N-00000277 -> (no net)
- P3 pad 2: /USB OTG/D- -> (no net)
- P3 pad 3: /USB OTG/D+ -> (no net)
- R3 pad 1: N-00000271 -> /Ethernet/+Filter
- R4 pad 1: N-00000271 -> /Ethernet/+Filter
- R5 pad 1: N-00000271 -> /Ethernet/+Filter
- R6 pad 1: N-00000271 -> /Ethernet/+Filter
- R98 pad 1: +3.3V -> Net-(R98-Pad1)
- R98 pad 2: N-0000097 -> +3.3V
- TR2 pad 1: /USB OTG/D- -> Net-(J6-Pad2)
- TR2 pad 4: /USB OTG/D+ -> Net-(J6-Pad3)
- U1 pad 1: N-00000271 -> /Ethernet/+Filter
- U1 pad 27: N-00000271 -> /Ethernet/+Filter
- U12 pad 1: N-00000230 -> GND
- U12 pad 2: N-00000231 -> GND
- U12 pad 3: N-00000237 -> +3.3V
- U13 pad 1: N-00000232 -> +3.3V
- U13 pad 2: N-00000233 -> GND
- U13 pad 3: N-00000234 -> GND
- U16 pad 23: /USB OTG/USB0_PWR_FAULT -> /CPU/SPI_SCK
- U16 pad 34: /CPU/SPI_SCK -> /USB OTG/USB0_PWR_FAULT
- U17 pad 14: N-0000097 -> Net-(R98-Pad1)
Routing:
- net GND: track 490.0 -> 140.3 mm, vias 114 -> 17
- net +3.3V: track 261.1 -> 76.1 mm, vias 65 -> 10
- net /Memorias NV/SPIFI_CLK: track 137.7 -> 0.00 mm, vias 8 -> 0
- net +5V: track 128.0 -> 7.48 mm, vias 18 -> 0
- net /USB OTG/USB0_PWR_FAULT: track 118.0 -> 0.00 mm, vias 5 -> 0
- net /USB OTG/USB0_PPWR: track 115.8 -> 0.00 mm, vias 3 -> 0
- net GNDA: track 132.6 -> 22.2 mm, vias 28 -> 2
- net /CPU/USB_VBUS: track 98.9 -> 4.78 mm, vias 5 -> 0
- net /CPU/RESET: track 95.4 -> 3.61 mm, vias 2 -> 1
- net /CPU/CAN_RD: track 82.3 -> 0.00 mm, vias 1 -> 0
- net /Entradas Digitales/COM: track 110.2 -> 29.0 mm, vias 7 -> 0
- net N-00000271: track 79.1 -> 0.00 mm, vias 5 -> 0
- net /CPU/PGED2: track 78.9 -> 0.00 mm, vias 1 -> 0
- net /USB OTG/D+: track 77.5 -> 0.00 mm, vias 2 -> 0
- net /USB OTG/D-: track 75.9 -> 0.00 mm, vias 2 -> 0
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- added copper zone on Inner2.Cu, net /CPU/USB_JTAG_1.8V
- added copper zone on F.Cu, net N-00000168
- added copper zone on F.Cu, net N-00000211
- added copper zone on F.Cu, net N-00000214
- added copper zone on B.Cu, net N-00000225
- added copper zone on B.Cu, net N-00000226
- added copper zone on B.Cu, net N-00000239
- added copper zone on B.Cu, net N-00000240
- added copper zone on F.Cu, net N-00000240
- added copper zone on B.Cu, net N-00000241
- added copper zone on F.Cu, net N-00000241
- added copper zone on B.Cu, net N-00000356
- added copper zone on F.Cu, net N-00000373
- added copper zone on F.Cu, net N-00000374
- added copper zone on F.Cu, net N-00000375
- added copper zone on F.Cu, net N-00000376
- added copper zone on F.Cu, net N-00000377
- added copper zone on F.Cu, net N-00000378
- added copper zone on F.Cu, net N-00000379
- added copper zone on F.Cu, net N-00000390
- removed copper zone on Inner2.Cu, net /JTAG/USB_JTAG_1.8V
- removed copper zone on B.Cu, net Net-(C16-Pad1)
- removed copper zone on F.Cu, net Net-(C16-Pad1)
- removed copper zone on F.Cu, net Net-(C25-Pad1)
- removed copper zone on F.Cu, net Net-(C26-Pad1)
- removed copper zone on B.Cu, net Net-(D2-Pad1)
- removed copper zone on B.Cu, net Net-(D3-Pad2)
- removed copper zone on F.Cu, net Net-(D3-Pad2)
- removed copper zone on F.Cu, net Net-(FB7-Pad1)
- removed copper zone on F.Cu, net Net-(J13-Pad1)
- removed copper zone on F.Cu, net Net-(J13-Pad2)
- removed copper zone on B.Cu, net Net-(J15-Pad1)
- removed copper zone on F.Cu, net Net-(J15-Pad2)
- removed copper zone on F.Cu, net Net-(J15-Pad3)
- removed copper zone on B.Cu, net Net-(J2-Pad1)
- removed copper zone on B.Cu, net Net-(J2-Pad2)
- removed copper zone on F.Cu, net Net-(Q2-Pad4)
- removed copper zone on F.Cu, net Net-(Q3-Pad4)
- removed copper zone on F.Cu, net Net-(Q4-Pad4)
- removed copper zone on F.Cu, net Net-(Q5-Pad4)
